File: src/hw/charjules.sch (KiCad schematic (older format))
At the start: 13 parts

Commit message: schéma (pour le plaisir du commit de fin de soirée, début de nuit :-)
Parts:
- added R? (x30): R, symbol Device:R
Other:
- moved on the sheet: R?

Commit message: un dernier pour la route
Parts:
- added C? (x10): C, symbol Device:C
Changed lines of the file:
@@
+	1    0    0    -1
+$EndComp
+$Comp
+L power:GND #PWR?
+U 1 1 5E172BE3
+P 6000 2450
+F 0 "#PWR?" H 6000 2200 50  0001 C CNN
+F 1 "GND" H 6005 2277 50  0000 C CNN
+F 2 "" H 6000 2450 50  0001 C CNN
+F 3 "" H 6000 2450 50  0001 C CNN
+	1    6000 2450
+	1    0    0    -1
+$EndComp
+$Comp
+L power:GND #PWR?
+U 1 1 5E179298
+P 6000 4900
+F 0 "#PWR?" H 6000 4650 50  0001 C CNN
+F 1 "GND" H 6005 4727 50  0000 C CNN
+F 2 "" H 6000 4900 50  0001 C CNN
+F 3 "" H 6000 4900 50  0001 C CNN
+	1    6000 4900
+	1    0    0    -1
+$EndComp
+$Comp
+L power:VDD #PWR?
+U 1 1 5E17AC79
+P 5850 900
+F 0 "#PWR?" H 5850 750 50  0001 C CNN
+F 1 "VDD" H 5867 1073 50  0000 C CNN
+F 2 "" H 5850 900 50  0001 C CNN
+F 3 "" H 5850 900 50  0001 C CNN
+	1    5850 900
+	1    0    0    -1
+$EndComp
+$Comp
+L power:VDD #PWR?
+U 1 1 5E17B39A
+P 5950 3300
+F 0 "#PWR?" H 5950 3150 50  0001 C CNN
+F 1 "VDD" H 5967 3473 50  0000 C CNN
+F 2 "" H 5950 3300 50  0001 C CNN
+F 3 "" H 5950 3300 50  0001 C CNN
+	1    5950 3300
+	1    0    0    -1
+$EndComp
+$Comp
+L Device:C C?
+U 1 1 5E17D535
+P 6950 4400
+F 0 "C?" H 7065 4446 50  0000 L CNN
+F 1 "C" H 7065 4355 50  0000 L CNN
+F 2 "" H 6988 4250 50  0001 C CNN
+F 3 "~" H 6950 4400 50  0001 C CNN
+	1    6950 4400
+	1    0    0    -1
+$EndComp
+$Comp
+L Device:C C?
+U 1 1 5E17E345
+P 7350 4400
+F 0 "C?" H 7465 4446 50  0000 L CNN
+F 1 "C" H 7465 4355 50  0000 L CNN
+F 2 "" H 7388 4250 50  0001 C CNN
+F 3 "~" H 7350 4400 50  0001 C CNN
+	1    7350 4400
+	1    0    0    -1
+$EndComp
+$Comp
+L Device:C C?
+U 1 1 5E17EB94
+P 7700 4400
+F 0 "C?" H 7815 4446 50  0000 L CNN
+F 1 "C" H 7815 4355 50  0000 L CNN
+F 2 "" H 7738 4250 50  0001 C CNN
+F 3 "~" H 7700 4400 50  0001 C CNN
+	1    7700 4400
+	1    0    0    -1
+$EndComp
+$Comp
+L Device:C C?
+U 1 1 5E17F30B
+P 8050 4400
+F 0 "C?" H 8165 4446 50  0000 L CNN
+F 1 "C" H 8165 4355 50  0000 L CNN
+F 2 "" H 8088 4250 50  0001 C CNN
+F 3 "~" H 8050 4400 50  0001 C CNN
+	1    8050 4400
+	1    0    0    -1
+$EndComp
+$Comp
+L Device:C C?
+U 1 1 5E180625
+P 8400 4400
+F 0 "C?" H 8515 4446 50  0000 L CNN
+F 1 "C" H 8515 4355 50  0000 L CNN
+F 2 "" H 8438 4250 50  0001 C CNN
+F 3 "~" H 8400 4400 50  0001 C CNN
+	1    8400 4400
+	1    0    0    -1
+$EndComp
+$Comp
+L Device:C C?
+U 1 1 5E185EFB
+P 6950 1950
+F 0 "C?" H 7065 1996 50  0000 L CNN
+F 1 "C" H 7065 1905 50  0000 L CNN
+F 2 "" H 6988 1800 50  0001 C CNN
+F 3 "~" H 6950 1950 50  0001 C CNN
+	1    6950 1950
+	1    0    0    -1
+$EndComp
+$Comp
+L Device:C C?
+U 1 1 5E185F05
+P 7350 1950
+F 0 "C?" H 7465 1996 50  0000 L CNN
+F 1 "C" H 7465 1905 50  0000 L CNN
+F 2 "" H 7388 1800 50  0001 C CNN
+F 3 "~" H 7350 1950 50  0001 C CNN
+	1    7350 1950
+	1    0    0    -1
+$EndComp
+$Comp
+L Device:C C?
+U 1 1 5E185F0F
+P 7700 1950
+F 0 "C?" H 7815 1996 50  0000 L CNN
+F 1 "C" H 7815 1905 50  0000 L CNN
+F 2 "" H 7738 1800 50  0001 C CNN
+F 3 "~" H 7700 1950 50  0001 C CNN
+	1    7700 1950
+	1    0    0    -1
+$EndComp
+$Comp
+L Device:C C?
+U 1 1 5E185F19
+P 8050 1950
+F 0 "C?" H 8165 1996 50  0000 L CNN
+F 1 "C" H 8165 1905 50  0000 L CNN
+F 2 "" H 8088 1800 50  0001 C CNN
+F 3 "~" H 8050 1950 50  0001 C CNN
+	1    8050 1950
+	1    0    0    -1
+$EndComp
+$Comp
+L Device:C C?
+U 1 1 5E185F23
+P 8400 1950
+F 0 "C?" H 8515 1996 50  0000 L CNN
+F 1 "C" H 8515 1905 50  0000 L CNN
+F 2 "" H 8438 1800 50  0001 C CNN
+F 3 "~" H 8400 1950 50  0001 C CNN
+	1    8400 1950
 	1    0    0    -1
 $EndComp

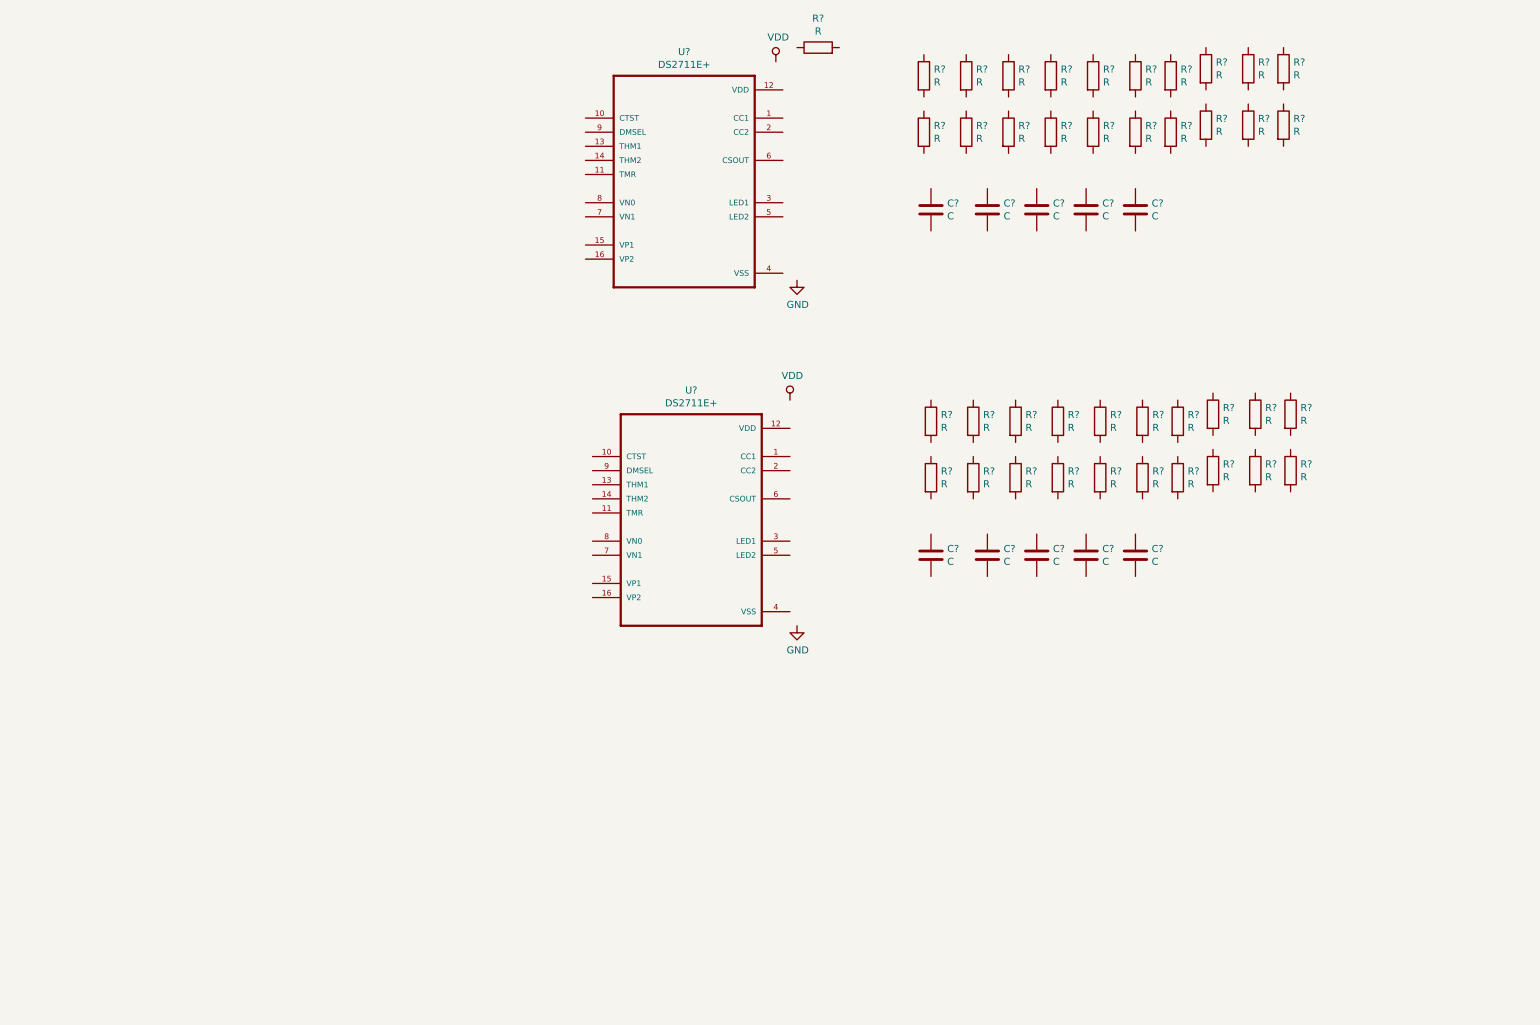
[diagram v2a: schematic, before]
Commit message: Ajout des transistors de charge Début de cablage Nombreux commentaires ajoutés dans la doc, et nombreuses questions aussi
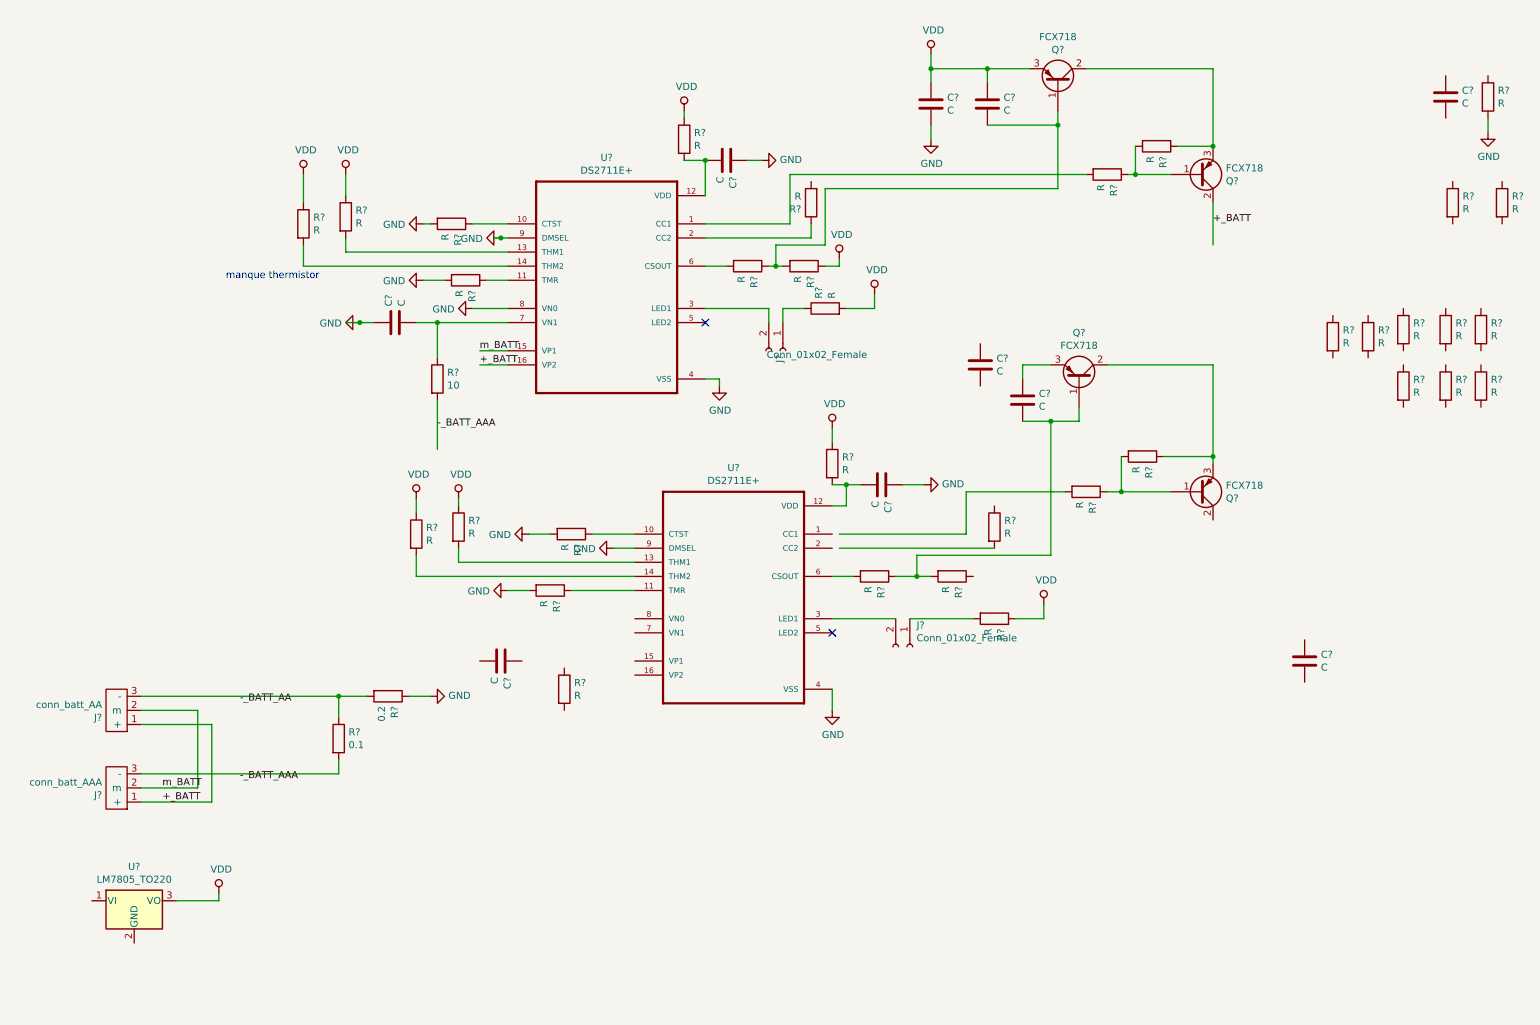
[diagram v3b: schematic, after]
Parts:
- removed R? (x4): R, symbol Device:R
- added J?: conn_batt_AAA, symbol f4bjh:conn_batt_AAA
- added J?: conn_batt_AA, symbol f4bjh:conn_batt_AA
- added J? (x2): Conn_01x02_Female, symbol Connector:Conn_01x02_Female
- added Q? (x4): FCX718, symbol f4bjh:FCX718
- added U?: LM7805_TO220, Package_TO_SOT_THT:TO-220-3_Vertical, symbol Regulator_Linear:LM7805_TO220
- R?: value R -> 10
- R?: value R -> 0.1
- R?: value R -> 0.2
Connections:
- net labels added: +_BATT, -_BATT_AA, -_BATT_AAA, m_BATT
- wire segments 0 -> 122
- no-connect marks 0 -> 2
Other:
- note added: "manque thermistor"
- moved on the sheet: C?, R?, U?

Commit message: Continue le cablage
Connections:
- net labels added: +_BATT_1, +_BATT_2, -_BATT_2, -_BATT_AAA_1, -_BATT_AA_1, m_BATT_1, m_BATT_2
- net labels removed: +_BATT, -_BATT_AA, -_BATT_AAA, m_BATT
- wire segments 122 -> 135
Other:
- note added: "Vérifier le schéma par rapport au fonctionnement du composant dans la spec\net vérifier le schéma par rapport à un schéma d'application du net\net vérifier le schéma par rapport à un schéma d'application de la spec"
- moved on the sheet: C?, R?
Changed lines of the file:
@@
 L Device:R R?
 U 1 1 5E168814
-P 4350 5350
-F 0 "R?" H 4420 5396 50  0000 L CNN
-F 1 "R" H 4420 5305 50  0000 L CNN
-F 2 "" V 4280 5350 50  0001 C CNN
-F 3 "~" H 4350 5350 50  0001 C CNN
-	1    4350 5350
+P 4250 5150
+F 0 "R?" H 4320 5196 50  0000 L CNN
+F 1 "R" H 4320 5105 50  0000 L CNN
+F 2 "" V 4180 5150 50  0001 C CNN
+F 3 "~" H 4250 5150 50  0001 C CNN
+	1    4250 5150
 	1    0    0    -1
 $EndComp
@@
 L Device:C C?
 U 1 1 5E17D535
-P 7300 3050
-F 0 "C?" H 7415 3096 50  0000 L CNN
-F 1 "C" H 7415 3005 50  0000 L CNN
-F 2 "" H 7338 2900 50  0001 C CNN
-F 3 "~" H 7300 3050 50  0001 C CNN
-	1    7300 3050
+P 7350 3250
+F 0 "C?" H 7465 3296 50  0000 L CNN
+F 1 "C" H 7465 3205 50  0000 L CNN
+F 2 "" H 7388 3100 50  0001 C CNN
+F 3 "~" H 7350 3250 50  0001 C CNN
+	1    7350 3250
 	1    0    0    -1
 $EndComp
@@
 L Device:C C?
 U 1 1 5E17F30B
-P 3900 5150
-F 0 "C?" H 4015 5196 50  0000 L CNN
-F 1 "C" H 4015 5105 50  0000 L CNN
-F 2 "" H 3938 5000 50  0001 C CNN
-F 3 "~" H 3900 5150 50  0001 C CNN
-	1    3900 5150
+P 4000 4950
+F 0 "C?" H 4115 4996 50  0000 L CNN
+F 1 "C" H 4115 4905 50  0000 L CNN
+F 2 "" H 4038 4800 50  0001 C CNN
+F 3 "~" H 4000 4950 50  0001 C CNN
+	1    4000 4950
 	0    1    1    0
 $EndComp
@@
 	1750 5500 1750 6050
 Text Label 1500 6150 0    50   ~ 0
-+_BATT
++_BATT_1
 Text Label 1500 6050 0    50   ~ 0
-m_BATT
+m_BATT_1
 Text Label 2050 6000 0    50   ~ 0
--_BATT_AAA
+-_BATT_AAA_1
 Wire Wire Line
 	1850 6150 1350 6150
@@
 	1750 5500 1350 5500
 Text Label 2050 5450 0    50   ~ 0
--_BATT_AA
+-_BATT_AA_1
 Wire Wire Line
 	8950 1900 8950 2200
 Text Label 8950 2050 0    50   ~ 0
-+_BATT
++_BATT_1
 Text Label 3750 2950 0    50   ~ 0
-m_BATT
+m_BATT_1
 Wire Wire Line
 	3950 3050 3750 3050
 Text Label 3750 3050 0    50   ~ 0
-+_BATT
++_BATT_1
 Connection ~ 2900 2750
 Wire Wire Line
@@
 	3450 3300 3450 3650
 Text Label 3450 3500 0    50   ~ 0
--_BATT_AAA
+-_BATT_AAA_1
 Wire Wire Line
 	2750 5400 2750 5550
@@
 L power:GND #PWR?
 U 1 1 5E5E19E3
-P 3400 5400
-F 0 "#PWR?" H 3400 5150 50  0001 C CNN
-F 1 "GND" V 3405 5272 50  0000 R CNN
-F 2 "" H 3400 5400 50  0001 C CNN
-F 3 "" H 3400 5400 50  0001 C CNN
-	1    3400 5400
+P 3500 5400
+F 0 "#PWR?" H 3500 5150 50  0001 C CNN
+F 1 "GND" V 3505 5272 50  0000 R CNN
+F 2 "" H 3500 5400 50  0001 C CNN
+F 3 "" H 3500 5400 50  0001 C CNN
+	1    3500 5400
 	0    -1   -1   0
 $EndComp
@@
 	2750 5400 2950 5400
 Connection ~ 2750 5400
-Wire Wire Line
-	3250 5400 3400 5400
 NoConn ~ 6250 4950
 Wire Wire Line
@@
 	6250 3500 6250 3600
 Wire Wire Line
-	6300 4250 7200 4250
-Wire Wire Line
 	7200 4250 7200 3950
 Wire Wire Line
@@
 Wire Wire Line
 	6700 4550 6850 4550
-Wire Wire Line
-	6300 4350 7400 4350
 Wire Wire Line
 	6850 4550 6850 4400
@@
 Wire Wire Line
 	3950 4650 4100 4650
+$Comp
+L power:GND #PWR?
+U 1 1 5E84023C
+P 3750 4950
+F 0 "#PWR?" H 3750 4700 50  0001 C CNN
+F 1 "GND" V 3755 4822 50  0000 R CNN
+F 2 "" H 3750 4950 50  0001 C CNN
+F 3 "" H 3750 4950 50  0001 C CNN
+	1    3750 4950
+	0    1    1    0
+$EndComp
+Wire Wire Line
+	3750 4950 3850 4950
+Wire Wire Line
+	3250 5400 3500 5400
+$Comp
+L power:GND #PWR?
+U 1 1 5E87D579
+P 4750 4850
+F 0 "#PWR?" H 4750 4600 50  0001 C CNN
+F 1 "GND" V 4755 4722 50  0000 R CNN
+F 2 "" H 4750 4850 50  0001 C CNN
+F 3 "" H 4750 4850 50  0001 C CNN
+	1    4750 4850
+	0    1    1    0
+$EndComp
+Wire Wire Line
+	4750 4850 4850 4850
+Wire Wire Line
+	4150 4950 4250 4950
+Wire Wire Line
+	4250 5000 4250 4950
+Connection ~ 4250 4950
+Wire Wire Line
+	4250 4950 4850 4950
+Wire Wire Line
+	4250 5300 4250 5550
+Wire Wire Line
+	4850 5150 4550 5150
+Wire Wire Line
+	4850 5250 4550 5250
+Text Label 4550 5150 0    50   ~ 0
+m_BATT_2
+Text Label 4600 5250 0    50   ~ 0
++_BATT_2
+Text Label 4250 5500 0    50   ~ 0
+-_BATT_2
+Wire Wire Line
+	8950 4150 8950 4550
+Text Label 8950 4500 0    50   ~ 0
++_BATT_2
+Wire Wire Line
+	6250 4250 7200 4250
+Wire Wire Line
+	6250 4350 7400 4350
+Text Notes 2800 4650 0    50   ~ 0
+manque thermistor
+$Comp
+L power:VDD #PWR?
+U 1 1 5E8D2F21
+P 7350 2950
+F 0 "#PWR?" H 7350 2800 50  0001 C CNN
+F 1 "VDD" H 7367 3123 50  0000 C CNN
+F 2 "" H 7350 2950 50  0001 C CNN
+F 3 "" H 7350 2950 50  0001 C CNN
+	1    7350 2950
+	1    0    0    -1
+$EndComp
+$Comp
+L power:GND #PWR?
+U 1 1 5E8D3B7C
+P 7350 3550
+F 0 "#PWR?" H 7350 3300 50  0001 C CNN
+F 1 "GND" H 7355 3377 50  0000 C CNN
+F 2 "" H 7350 3550 50  0001 C CNN
+F 3 "" H 7350 3550 50  0001 C CNN
+	1    7350 3550
+	1    0    0    -1
+$EndComp
+Wire Wire Line
+	7350 2950 7350 3050
+Wire Wire Line
+	7350 3400 7350 3550
+Wire Wire Line
+	7600 3050 7350 3050
+Connection ~ 7600 3050
+Connection ~ 7350 3050
+Wire Wire Line
+	7350 3050 7350 3100
+Text Notes 7550 5800 0    50   ~ 0
+Vérifier le schéma par rapport au fonctionnement du composant dans la spec\net vérifier le schéma par rapport à un schéma d'application du net\net vérifier le schéma par rapport à un schéma d'application de la spec
 $EndSCHEMATC
